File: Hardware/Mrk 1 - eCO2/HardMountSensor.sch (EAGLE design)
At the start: 12 parts, among them J2 SOLDERCUP_CONN_QUAD, Q1 DMG3404, U1 SPG30, U2 SHTC3DFN, U3 TPS7A0518DBV, U4 TXS0102DCU

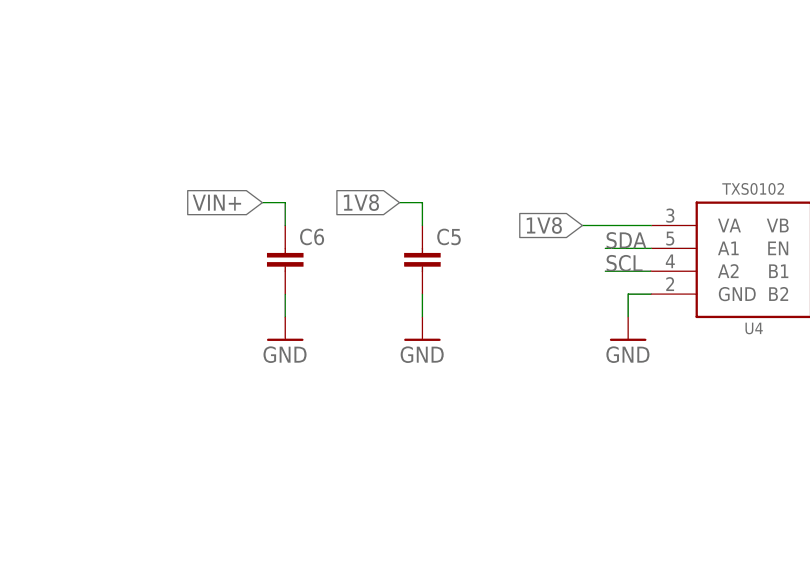
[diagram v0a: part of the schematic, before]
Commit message: Updated/generated BoMs if not present
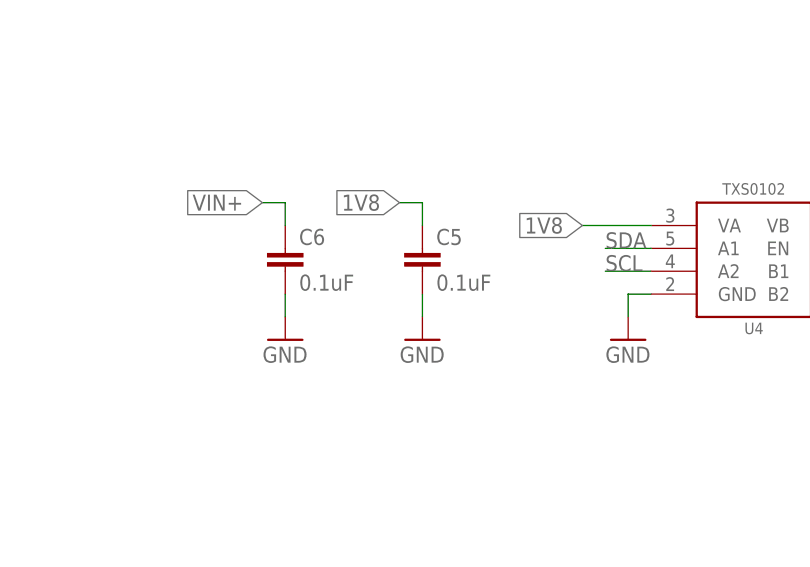
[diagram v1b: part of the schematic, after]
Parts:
- C5, C6: value (none) -> 0.1uF
- U3: DIGIKEY (none) -> 1649-1015-1-ND
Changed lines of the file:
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@@
 <part name="GND2" library="supply1" library_urn="urn:adsk.eagle:library:371" deviceset="GND" device=""/>
 <part name="C2" library="bschulz_passives" deviceset="C-EU" device="C0603" technology="0.1UF" value="0.1uF"/>
-<part name="U3" library="bschulz" deviceset="TPS7A05*" device="DBV" technology="18"/>
+<part name="U3" library="bschulz" deviceset="TPS7A05*" device="DBV" technology="18">
+<attribute name="DIGIKEY" value="1649-1015-1-ND"/>
+</part>
 <part name="C3" library="bschulz_passives" deviceset="C-EU" device="C0603" technology="1UF" value="1uF"/>
 <part name="C4" library="bschulz_passives" deviceset="C-EU" device="C0603" technology="1UF" value="1uF"/>
@@
 <part name="U4" library="bschulz" deviceset="TXS0102" device="DCU"/>
 <part name="GND5" library="supply1" library_urn="urn:adsk.eagle:library:371" deviceset="GND" device=""/>
-<part name="C5" library="bschulz_passives" deviceset="C-EU" device="C0603" technology="0.1UF"/>
+<part name="C5" library="bschulz_passives" deviceset="C-EU" device="C0603" technology="0.1UF" value="0.1uF"/>
 <part name="GND6" library="supply1" library_urn="urn:adsk.eagle:library:371" deviceset="GND" device=""/>
-<part name="C6" library="bschulz_passives" deviceset="C-EU" device="C0603" technology="0.1UF"/>
+<part name="C6" library="bschulz_passives" deviceset="C-EU" device="C0603" technology="0.1UF" value="0.1uF"/>
 <part name="GND7" library="supply1" library_urn="urn:adsk.eagle:library:371" deviceset="GND" device=""/>
 <part name="Q1" library="bschulz" deviceset="MOSFET-NCH" device="-DMG3404L" value="DMG3404"/>
